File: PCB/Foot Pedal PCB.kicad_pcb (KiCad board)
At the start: 2 copper layers, 86 x 30 mm, 10 parts, among them J1 Conn_01x03_Female, SW1 SW_Push, SW2 SW_Push, SW3 SW_Push, U1 ProMicro

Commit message: PCB changes and incremental readme writes
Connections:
- net Net-(C1-Pad2) renamed /ROW0
- net Net-(D1-Pad1) renamed /LED1
- net Net-(D2-Pad1) renamed /LED2
- net Net-(J1-Pad3) renamed /COL2
- net Net-(R1-Pad1) renamed VCC
- net Net-(SW2-Pad1) renamed /COL0
- net Net-(SW3-Pad1) renamed /COL1

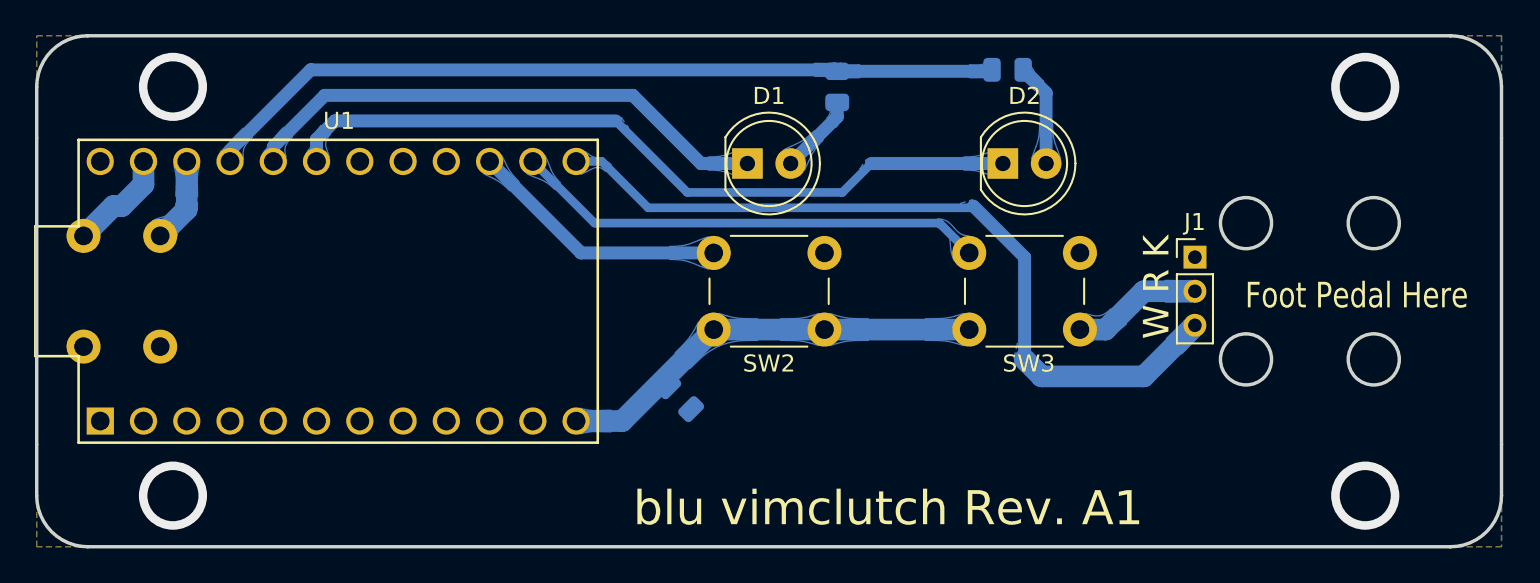
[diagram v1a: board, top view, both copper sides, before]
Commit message: Redid mounting holes for manufacturability.  Edge cuts are a no-go for the zip tie holes.
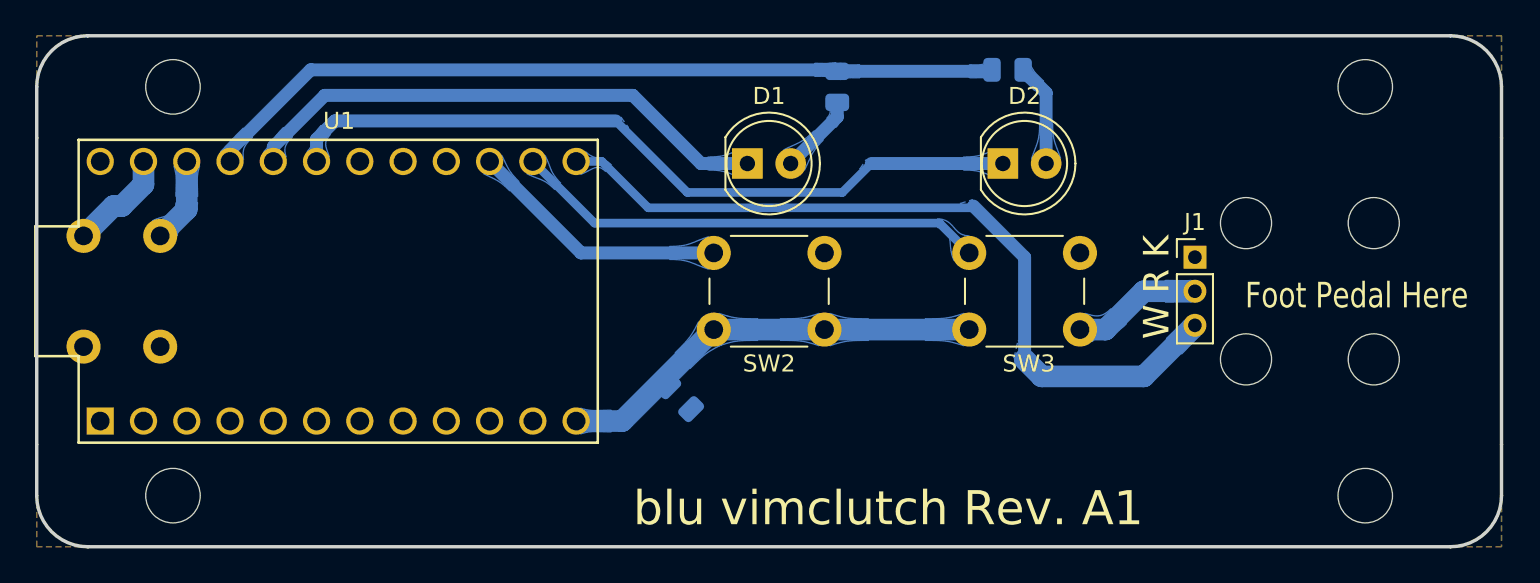
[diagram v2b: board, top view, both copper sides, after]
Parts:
- added ?: , , F.Cu at (108.8, 122.0)
- added ?: , , F.Cu at (171.8, 114.0)
- added ?: , , F.Cu at (108.8, 98.0)
- added ?: , , F.Cu at (179.2, 106.0)
- added ?: , , F.Cu at (171.8, 106.0)
- added ?: , , F.Cu at (178.8, 98.0)
- added REF**: MountingHole_3.2mm_M3, MountingHole:MountingHole_3.2mm_M3, F.Cu at (178.8, 122.0)
- added REF**: MountingHole_3mm, MountingHole:MountingHole_3mm, F.Cu at (179.2, 114.0)
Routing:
- net (no net): vias 4 -> 0
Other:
- outline, holes or cut-outs redrawn
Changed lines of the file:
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@@
     )
+  )
+  (footprint "" (layer "F.Cu")
+    (at 108.75 122)
+    (fp_text reference "" (at 0 0) (layer "F.SilkS")
+      (effects (font (size 1.27 1.27) (thickness 0.15)))
+    )
+    (fp_text value "" (at 0 0) (layer "F.SilkS")
+      (effects (font (size 1.27 1.27) (thickness 0.15)))
+    )
+    (pad "" np_thru_hole circle (at 0 0) (size 3.2 3.2) (drill 3.2) (layers *.Cu *.Mask))
   )
   (footprint "LED_THT:LED_D5.0mm" (layer "F.Cu")
@@
       (rotate (xyz 0 0 0))
     )
+  )
+  (footprint "" (layer "F.Cu")
+    (at 171.75 114)
+    (fp_text reference "" (at 0 0) (layer "F.SilkS")
+      (effects (font (size 1.27 1.27) (thickness 0.15)))
+    )
+    (fp_text value "" (at 0 0) (layer "F.SilkS")
+      (effects (font (size 1.27 1.27) (thickness 0.15)))
+    )
+    (pad "" np_thru_hole circle (at 0 0) (size 3 3) (drill 3) (layers *.Cu *.Mask))
   )
   (footprint "LED_THT:LED_D5.0mm" (layer "F.Cu")
@@
       (rotate (xyz 0 0 0))
     )
+  )
+  (footprint "MountingHole:MountingHole_3.2mm_M3" (layer "F.Cu")
+    (at 178.75 122)
+    (descr "Mounting Hole 3.2mm, no annular, M3")
+    (tags "mounting hole 3.2mm no annular m3")
+    (attr exclude_from_pos_files exclude_from_bom)
+    (fp_text reference "REF**" (at 0 -4.2) (layer "F.Fab")
+      (effects (font (size 1 1) (thickness 0.15)))
+    )
+    (fp_text value "MountingHole_3.2mm_M3" (at 0 4.2) (layer "F.Fab")
+      (effects (font (size 1 1) (thickness 0.15)))
+    )
+    (fp_circle (center 0 0) (end 3.2 0) (layer "Cmts.User") (width 0.15) (fill none))
+    (fp_circle (center 0 0) (end 3.45 0) (layer "F.CrtYd") (width 0.05) (fill none))
+    (pad "" np_thru_hole circle (at 0 0) (size 3.2 3.2) (drill 3.2) (layers *.Cu *.Mask))
+  )
+  (footprint "" (layer "F.Cu")
+    (at 108.75 98)
+    (fp_text reference "" (at 0 0) (layer "F.SilkS")
+      (effects (font (size 1.27 1.27) (thickness 0.15)))
+    )
+    (fp_text value "" (at 0 0) (layer "F.SilkS")
+      (effects (font (size 1.27 1.27) (thickness 0.15)))
+    )
+    (pad "" np_thru_hole circle (at 0 0) (size 3.2 3.2) (drill 3.2) (layers *.Cu *.Mask))
+  )
+  (footprint "" (layer "F.Cu")
+    (at 179.25 106)
+    (fp_text reference "" (at 0 0) (layer "F.SilkS")
+      (effects (font (size 1.27 1.27) (thickness 0.15)))
+    )
+    (fp_text value "" (at 0 0) (layer "F.SilkS")
+      (effects (font (size 1.27 1.27) (thickness 0.15)))
+    )
+    (pad "" np_thru_hole circle (at 0 0) (size 3 3) (drill 3) (layers *.Cu *.Mask))
   )
   (footprint "Promicro':ProMicro" (layer "F.Cu")
@@
       (net 21 "unconnected-(U1-Pad24)") (pinfunction "RAW") (pintype "power_out+no_connect"))
   )
+  (footprint "MountingHole:MountingHole_3mm" (layer "F.Cu")
+    (at 179.25 114)
+    (descr "Mounting Hole 3mm, no annular")
+    (tags "mounting hole 3mm no annular")
+    (attr exclude_from_pos_files exclude_from_bom)
+    (fp_text reference "REF**" (at 0 -4) (layer "F.Fab")
+      (effects (font (size 1 1) (thickness 0.15)))
+    )
+    (fp_text value "MountingHole_3mm" (at 0 4) (layer "F.Fab")
+      (effects (font (size 1 1) (thickness 0.15)))
+    )
+    (fp_text user "${REFERENCE}" (at 0 0) (layer "F.Fab")
+      (effects (font (size 1 1) (thickness 0.15)))
+    )
+    (fp_circle (center 0 0) (end 3 0) (layer "Cmts.User") (width 0.15) (fill none))
+    (fp_circle (center 0 0) (end 3.25 0) (layer "F.CrtYd") (width 0.05) (fill none))
+    (pad "" np_thru_hole circle (at 0 0) (size 3 3) (drill 3) (layers *.Cu *.Mask))
+  )
+  (footprint "" (layer "F.Cu")
+    (at 171.75 106)
+    (fp_text reference "" (at 0 0) (layer "F.SilkS")
+      (effects (font (size 1.27 1.27) (thickness 0.15)))
+    )
+    (fp_text value "" (at 0 0) (layer "F.SilkS")
+      (effects (font (size 1.27 1.27) (thickness 0.15)))
+    )
+    (pad "" np_thru_hole circle (at 0 0) (size 3 3) (drill 3) (layers *.Cu *.Mask))
+  )
+  (footprint "" (layer "F.Cu")
+    (at 178.75 98)
+    (fp_text reference "" (at 0 0) (layer "F.SilkS")
+      (effects (font (size 1.27 1.27) (thickness 0.15)))
+    )
+    (fp_text value "" (at 0 0) (layer "F.SilkS")
+      (effects (font (size 1.27 1.27) (thickness 0.15)))
+    )
+    (pad "" np_thru_hole circle (at 0 0) (size 3.2 3.2) (drill 3.2) (layers *.Cu *.Mask))
+  )
   (footprint "Button_Switch_THT:SW_PUSH_6mm_H5mm" (layer "F.Cu")
     (at 155.5 107.75)
@@
   (gr_rect (start 177.5 112.25) (end 181 116.25) (layer "B.SilkS") (width 0.15) (fill none))
   (gr_rect (start 170 107.75) (end 173.5 103.75) (layer "B.SilkS") (width 0.15) (fill none))
-  (gr_circle (center 171.75 114) (end 173.25 114) (layer "Edge.Cuts") (width 0.2) (fill none))
   (gr_line (start 100.75 98) (end 100.75 101) (layer "Edge.Cuts") (width 0.2))
   (gr_line (start 186.75 119) (end 186.75 122) (layer "Edge.Cuts") (width 0.2))
@@
   (gr_line (start 186.75 101) (end 186.75 98) (layer "Edge.Cuts") (width 0.2))
   (gr_line (start 183.75 125) (end 103.75 125) (layer "Edge.Cuts") (width 0.2))
-  (gr_circle (center 171.75 106) (end 173.25 106) (layer "Edge.Cuts") (width 0.2) (fill none))
   (gr_line (start 100.75 122) (end 100.75 119) (layer "Edge.Cuts") (width 0.2))
-  (gr_circle (center 179.25 106) (end 180.75 106) (layer "Edge.Cuts") (width 0.2) (fill none))
   (gr_arc (start 100.75 98) (mid 101.62868 95.87868) (end 103.75 95) (layer "Edge.Cuts") (width 0.2))
-  (gr_circle (center 179.249997 114) (end 180.749997 114) (layer "Edge.Cuts") (width 0.2) (fill none))
   (gr_line (start 100.75 119) (end 100.75 101) (layer "Edge.Cuts") (width 0.2))
   (gr_arc (start 186.75 122) (mid 185.87132 124.12132) (end 183.75 125) (layer "Edge.Cuts") (width 0.2))
@@
     (effects (font (size 1.5 1.2) (thickness 0.25)))
   )
-  (via (at 108.75 122) (size 4) (drill 3) (layers "F.Cu" "B.Cu") (free) (net 0))
-  (via (at 178.75 98) (size 4) (drill 3) (layers "F.Cu" "B.Cu") (free) (net 0))
-  (via (at 108.75 98) (size 4) (drill 3) (layers "F.Cu" "B.Cu") (free) (net 0))
-  (via (at 178.75 122) (size 4) (drill 3) (layers "F.Cu" "B.Cu") (free) (net 0))
   (segment (start 163.5 112.25) (end 165.75 110) (width 1.27) (layer "B.Cu") (net 2))
   (segment (start 165.75 110) (end 168.75 110) (width 1.27) (layer "B.Cu") (net 2))

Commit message: Added PDF and SVG plots of the schematic and PCB layers.  Added revision B which has direct pull-down on all keys.
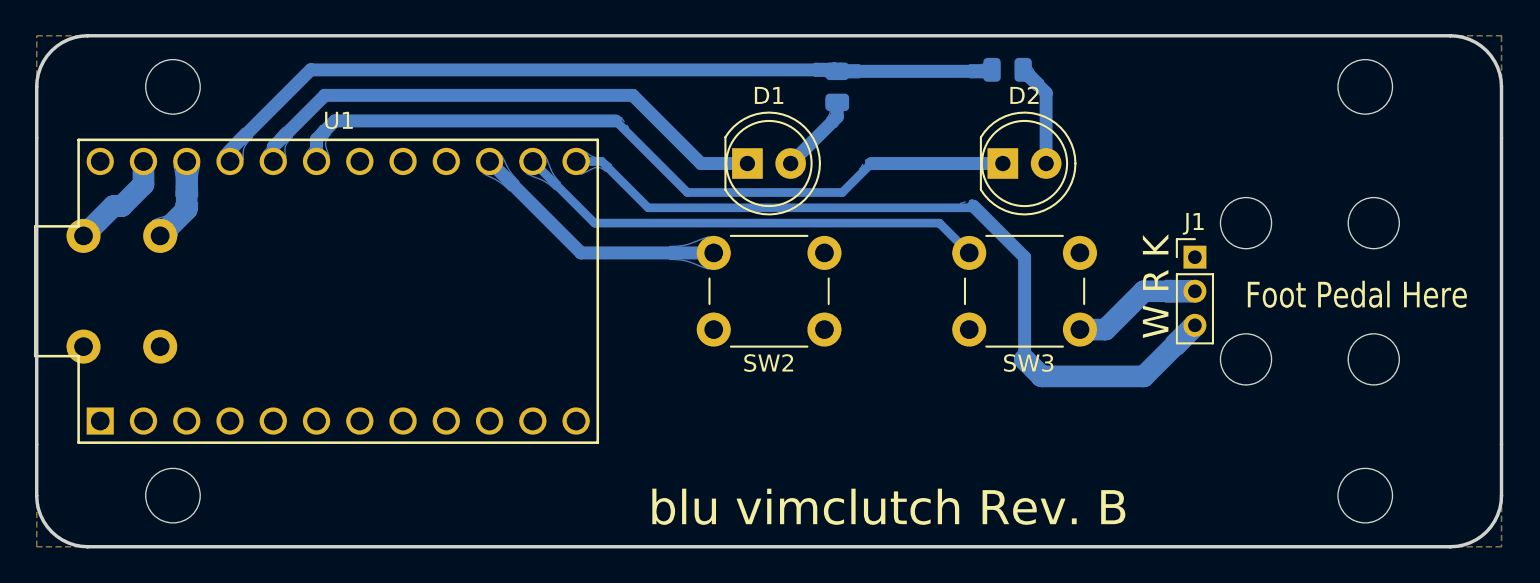
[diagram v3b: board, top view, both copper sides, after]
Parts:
- removed C1: UNP, Capacitor_SMD:C_0805_2012Metric
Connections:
- J1 pad 2: /ROW0 -> GND
- SW2 pad 2: /ROW0 -> GND
- SW3 pad 2: /ROW0 -> GND
- U1 pad 12: /ROW0 -> unconnected-(U1-B5-Pad12)
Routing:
- net /ROW0: track 33.0 -> 0.00 mm
- net GND: track 6.12 -> 13.8 mm
